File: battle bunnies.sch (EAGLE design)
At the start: 59 parts, among them IC1 CP2104, Q1 mmbt2222, Q2 mmbt2222, SW2 KMR2, U1 PCA9685, U2 SPX3819, U3 MCP73831T-2ACI/OT, X2 ESP-12, X4 20329

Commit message: Fixing Power LED
Right now the 'Power LED' is run from Ground to... Ground, so it's
not exactly going to work 'right'.  When moving things around in
Eagle it didn't attach properly to the 3.3V line on the schematic
and so was left dangling, despite it being connected.

This, thankfully, doesn't affect the boards except cause a little
bit of build waste.  This is fixed now, though it'll likely get
set to DNI, as it's only really useful on dev boards.
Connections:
- removed net N$11: D4.A
- net 3.3V: now also D4.A
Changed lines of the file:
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@@
 <pinref part="U2" gate="G$1" pin="OUT"/>
 <pinref part="U$10" gate="G$1" pin="3.3V"/>
+<pinref part="D4" gate="G$1" pin="A"/>
+<wire x1="73.66" y1="241.3" x2="68.58" y2="241.3" width="0.1524" layer="91"/>
 </segment>
 <segment>
@@
 </segment>
 </net>
-<net name="N$11" class="0">
-<segment>
-<wire x1="68.58" y1="241.3" x2="73.66" y2="241.3" width="0.1524" layer="91"/>
-<pinref part="D4" gate="G$1" pin="A"/>
-</segment>
-</net>

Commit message: Updating GPIO Table to actually be correct with the schematic
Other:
- note added: "GPIO Table (What's Used, What's Available) ------------------------ GPIO0 - LED (schematic) GPIO02/ - Strap GPIO4/SDA/PWM - PCA9865 GPIO5/SCL/IR Rx - IR Rx GPIO9 - GPIO10 - GPIO12/MISO/PWM/IR Tx - IR Tx GPIO13/MOSI - Button GPIO14/SCL/PWM - PCA9865 GPIO15/CS/PWM - GPIO16 (No Interrupts) - Button ADC - Should get routed back to VBAT Total: 17 GPIOs, 2 taken for UART (15). I count 14 pinned now"
- note removed: "GPIO Table (What's Used, What's Available) ------------------------ GPIO0 - LED (schematic) GPIO02/ - GPIO4/SDA/PWM - GPIO5/SCL/IR Rx - IR Rx GPIO9 - PCA9865 GPIO10 - PCA9865 GPIO12/MISO/PWM/IR Tx - IR Tx GPIO13/MOSI - GPIO14/SCL/PWM - GPIO15/CS/PWM - Button GPIO16 - Button ADC - Total: 17 GPIOs, 2 taken for UART (15). I count 14 pinned now"
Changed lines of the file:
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@@
 What's Available)
 ------------------------
-GPIO0             - LED (schematic)
-GPIO02/           -
-GPIO4/SDA/PWM     -
-GPIO5/SCL/IR Rx      - IR Rx
-GPIO9             - PCA9865
-GPIO10           - PCA9865
+GPIO0                           - LED (schematic)
+GPIO02/                        - Strap
+GPIO4/SDA/PWM            - PCA9865
+GPIO5/SCL/IR Rx             - IR Rx
+GPIO9                            -
+GPIO10                          -
 GPIO12/MISO/PWM/IR Tx - IR Tx
-GPIO13/MOSI -
-GPIO14/SCL/PWM   -
-GPIO15/CS/PWM     - Button
-GPIO16           - Button
-ADC                -
+GPIO13/MOSI                  - Button
+GPIO14/SCL/PWM            - PCA9865
+GPIO15/CS/PWM              -
+GPIO16 (No Interrupts)     - Button
+ADC                                - Should get routed back to VBAT
 Total: 17 GPIOs, 2 taken for UART (15).
 I count 14 pinned now</text>

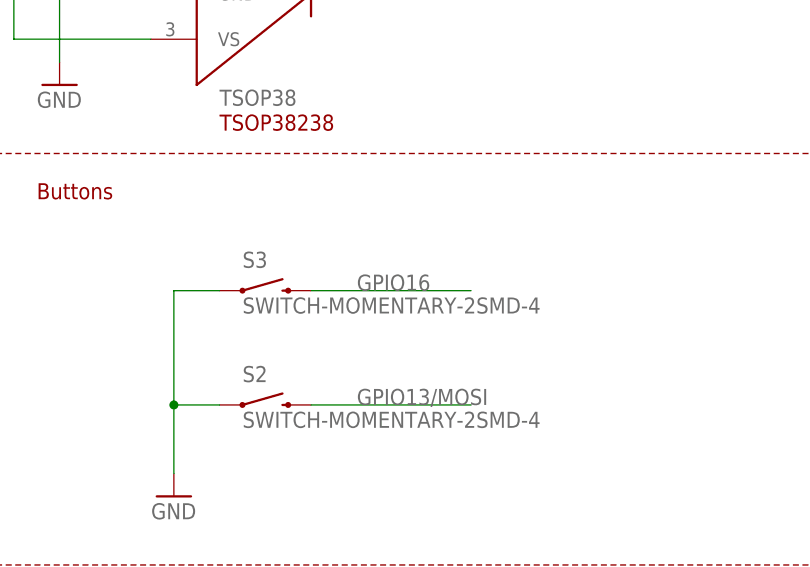
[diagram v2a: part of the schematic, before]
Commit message: Flipping GPIO16 with GPIO15 on the 'Battle' Button
GPIO16 *APPARENTLY* doesn't actually have hard interrupt
support, which makes it slightly obnoxious for the 'battle'
button, which should be there to wake the bunny from a sleep
state, or get it to do something.
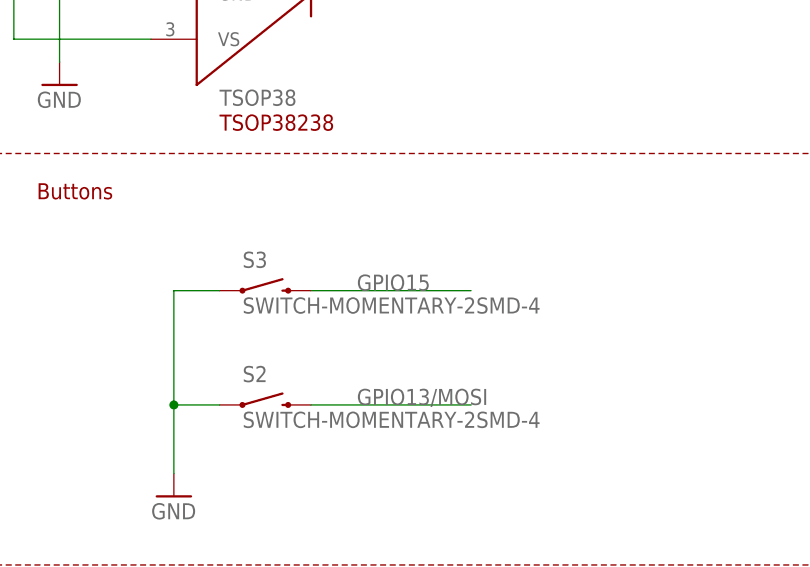
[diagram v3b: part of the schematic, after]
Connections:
- net GPIO15: now also S3.2
- net GPIO16: no longer S3.2
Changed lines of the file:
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@@
 <pinref part="JP2" gate="A" pin="9"/>
-</segment>
-<segment>
-<pinref part="S3" gate="G$1" pin="2"/>
-<wire x1="172.72" y1="76.2" x2="190.5" y2="76.2" width="0.1524" layer="91"/>
-<label x="177.8" y="76.2" size="1.778" layer="95"/>
 </segment>
 </net>
@@
 <pinref part="JP2" gate="A" pin="7"/>
 </segment>
+<segment>
+<pinref part="S3" gate="G$1" pin="2"/>
+<wire x1="172.72" y1="76.2" x2="190.5" y2="76.2" width="0.1524" layer="91"/>
+<label x="177.8" y="76.2" size="1.778" layer="95"/>
+</segment>
 </net>

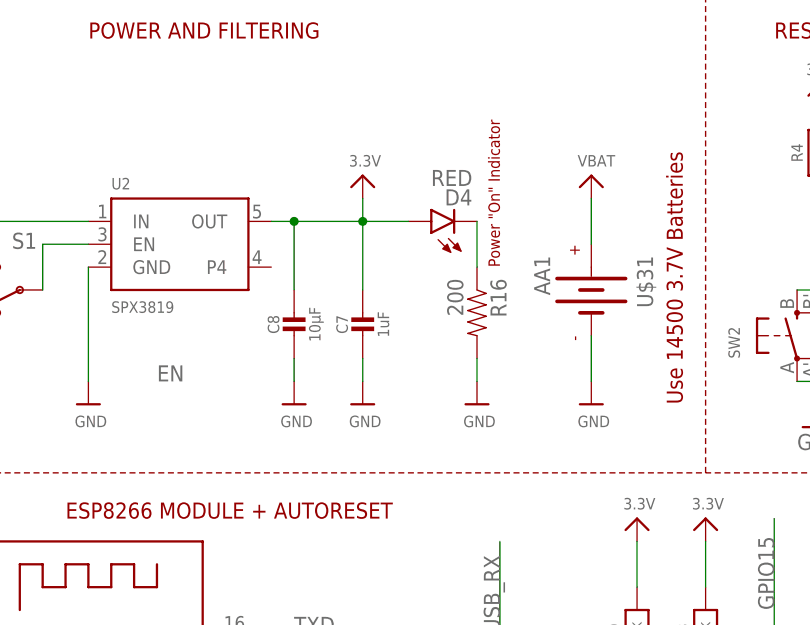
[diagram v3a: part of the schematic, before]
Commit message: Marking the "Power On" LEDs as DNI
They aren't needed and adding them is more a debugging
nicety vs. a critical need.
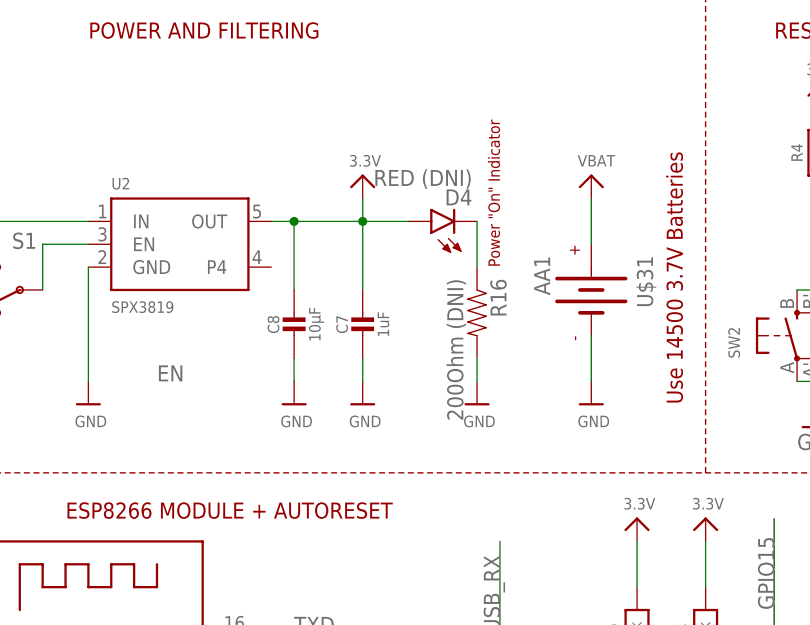
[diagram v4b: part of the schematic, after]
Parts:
- D4: value RED -> RED (DNI)
- R16: value 200 -> 200Ohm (DNI)
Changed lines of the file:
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@@
 <parts>
 <part name="FRAME1" library="frames" deviceset="TABL_L" device=""/>
-<part name="R16" library="SparkFun-Resistors" deviceset="200OHM1/10W1%(0603)" device="" value="200"/>
+<part name="R16" library="SparkFun-Resistors" deviceset="200OHM1/10W1%(0603)" device="" value="200Ohm (DNI)"/>
 <part name="S1" library="SparkFun-Electromechanical" deviceset="SWITCH-SPDT" device="-SMD-A">
 <attribute name="PROD_ID" value="SWCH-10651"/>
 </part>
-<part name="D4" library="SparkFun-LED" deviceset="LED-RED" device="0603" value="RED"/>
+<part name="D4" library="SparkFun-LED" deviceset="LED-RED" device="0603" value="RED (DNI)"/>
 <part name="R1" library="SparkFun-Resistors" deviceset="1KOHM-1/10W-1%(0603)" device="" value="1K"/>
 <part name="R15" library="SparkFun-Resistors" deviceset="1KOHM-1/10W-1%(0603)" device="" value="1K"/>
